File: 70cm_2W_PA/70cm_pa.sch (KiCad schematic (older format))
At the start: 47 parts, among them J3 Conn_01x02, U1 M68710L, U2 MIC5205YM5, U3 SN74LV1T08

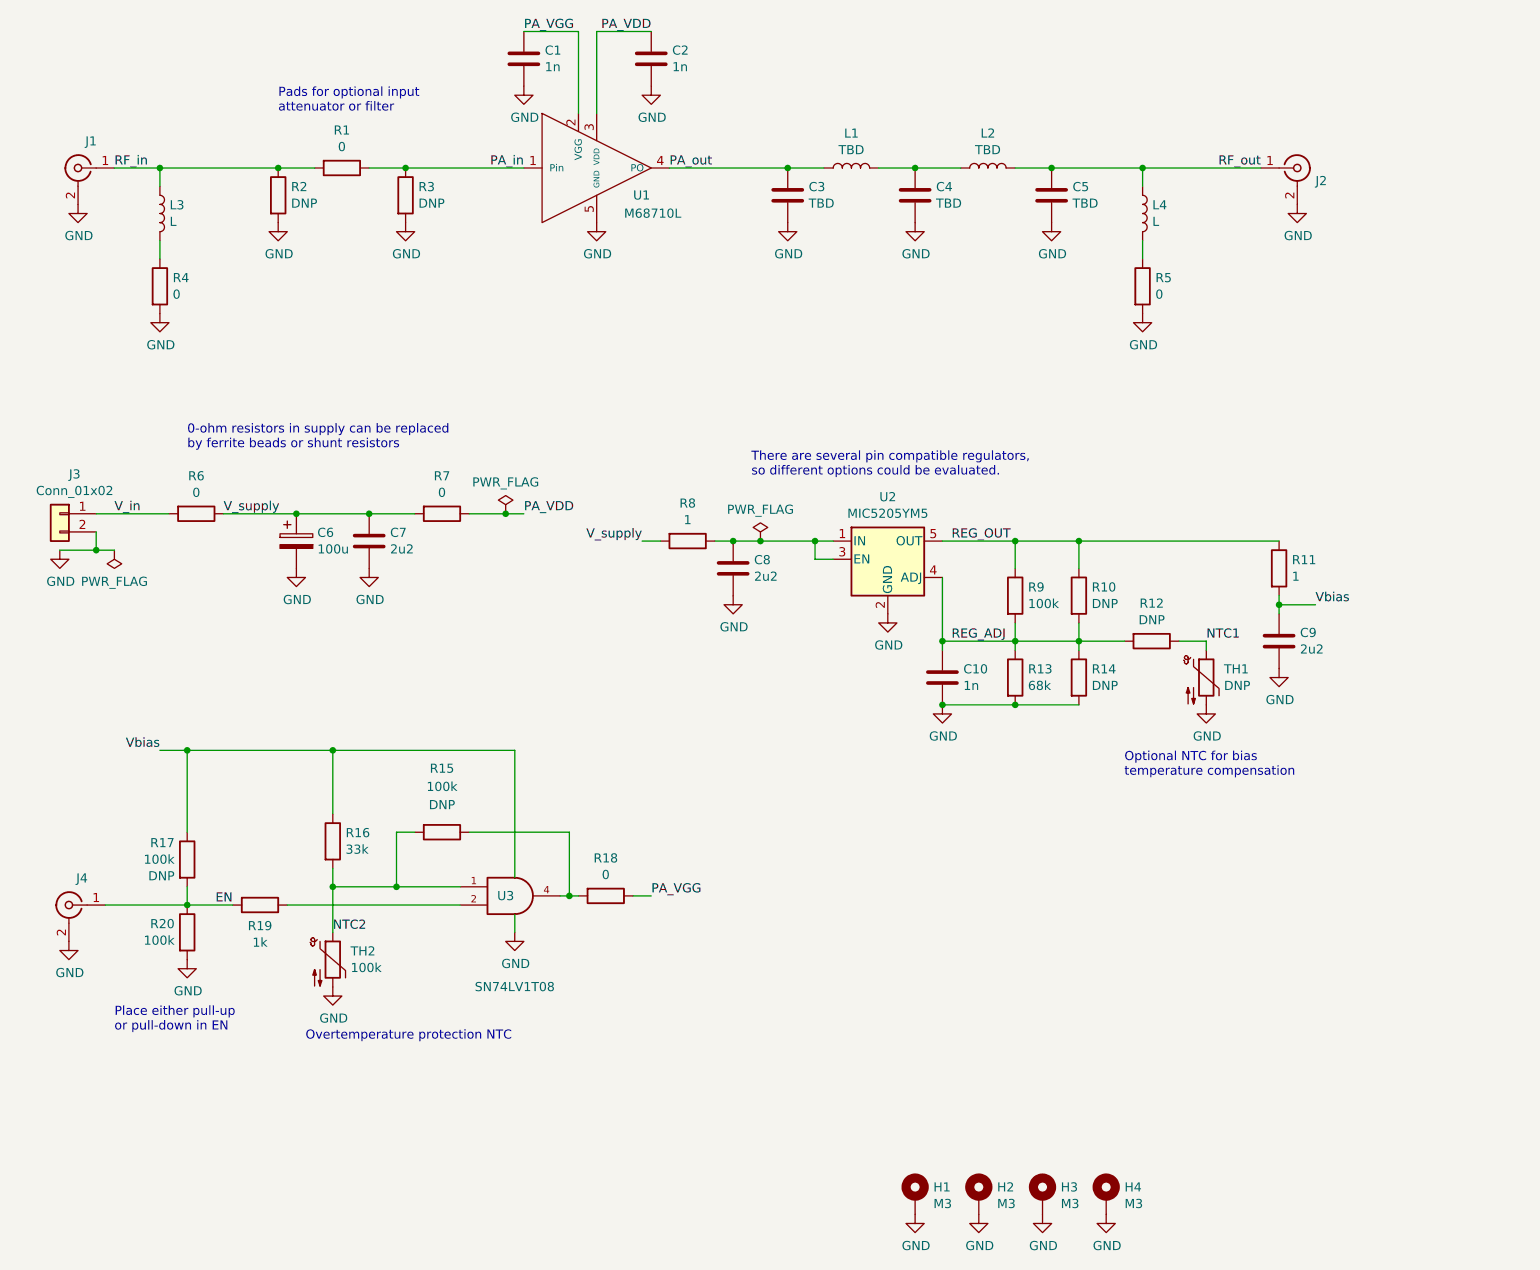
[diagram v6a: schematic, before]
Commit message: M68710L: Add more filtering and improve layout
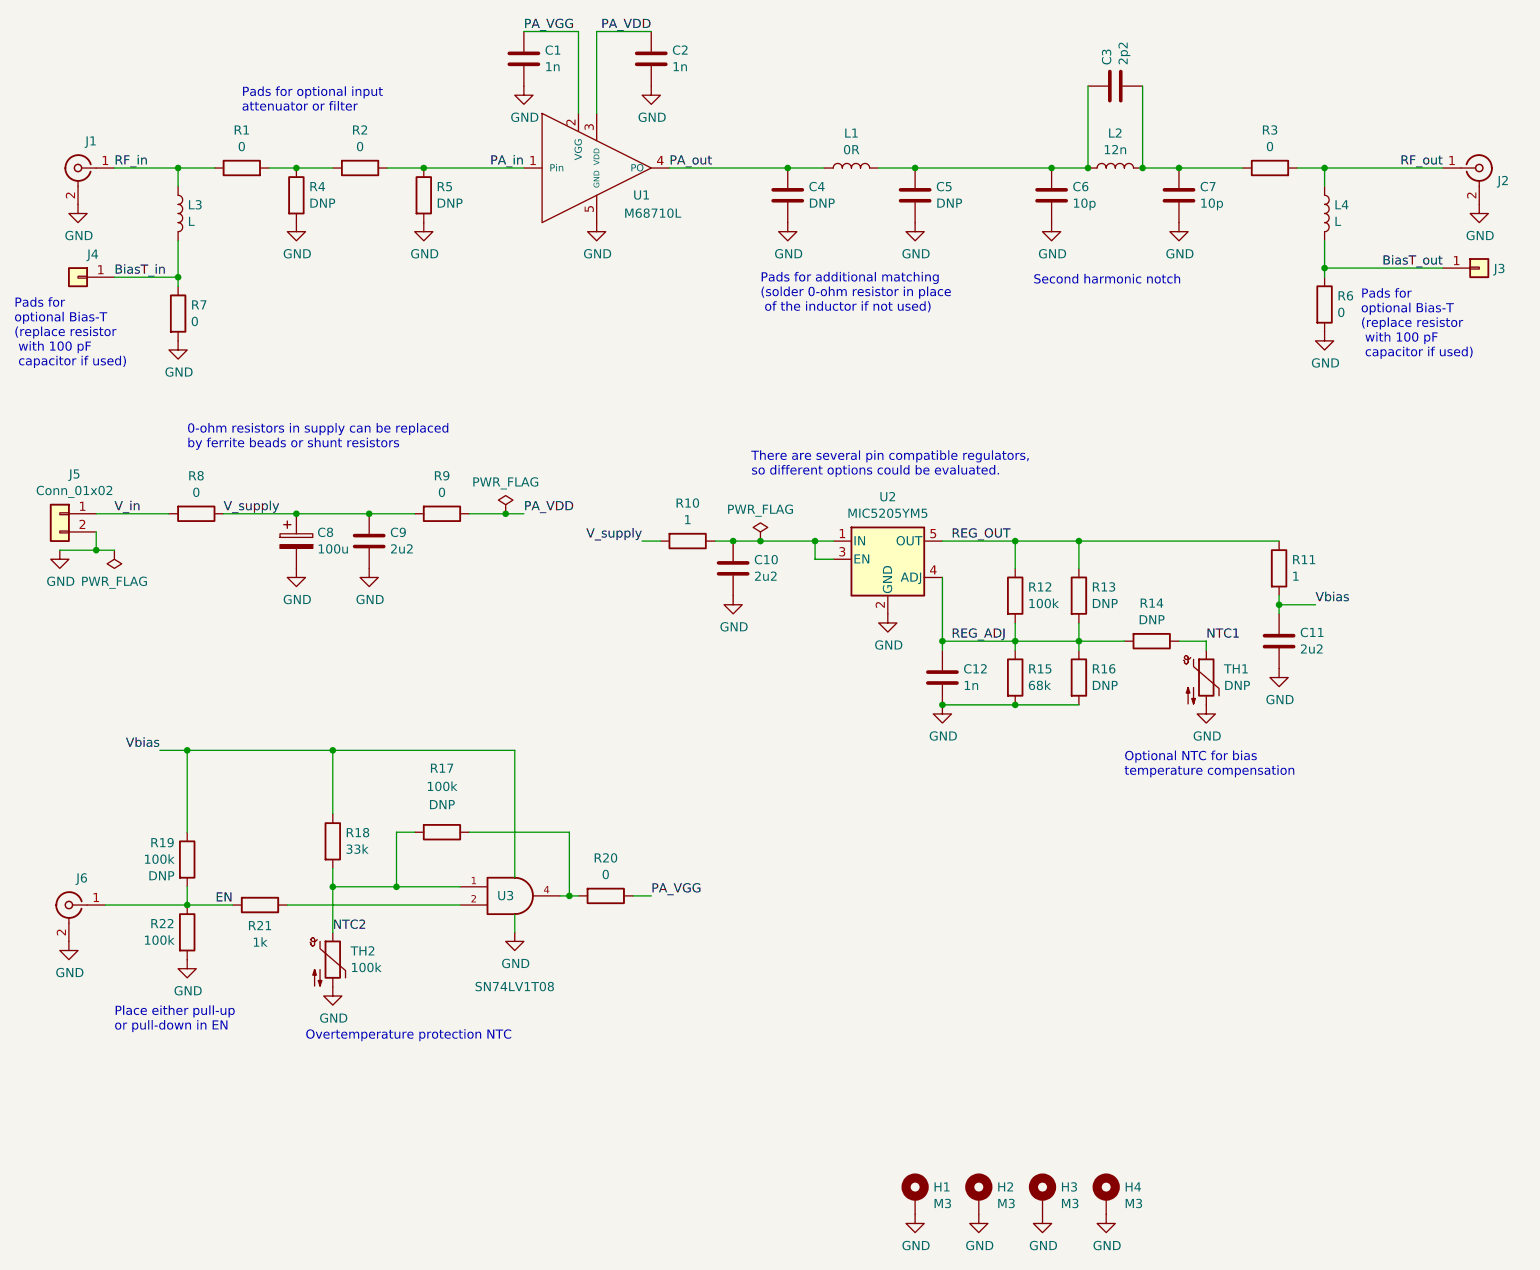
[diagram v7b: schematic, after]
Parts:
- added C3: 2p2, Capacitor_SMD:C_0805_2012Metric, symbol Device:C
- added C6: 10p, Capacitor_SMD:C_0805_2012Metric, symbol Device:C
- added J3, J4: ~, TestPoint:TestPoint_Pad_3.0x3.0mm, symbol Connector_Generic:Conn_01x01
- added R1, R3: 0, Resistor_SMD:R_0805_2012Metric, symbol Device:R
- C4: renamed from C3; value TBD -> ~; DNP (none) -> DNP
- C5: renamed from C4; value TBD -> ~; DNP (none) -> DNP
- C7: renamed from C5; value TBD -> 10p
- L1: value TBD -> 0R
- L2: value TBD -> 12n
- renumbered C8 to C10, C9 to C11, C10 to C12, C6 to C8, C7 to C9, J3 to J5, J4 to J6, R8 to R10, R9 to R12, R10 to R13, R12 to R14, R13 to R15, R14 to R16, R15 to R17, R16 to R18, R17 to R19, R1 to R2, R18 to R20, R19 to R21, R20 to R22, R2 to R4, R3 to R5, R5 to R6, R4 to R7, R6 to R8, R7 to R9
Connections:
- net GND: now also C6.2
- net RF_in: now also R1.1; no longer R2.2, R4.1
- net RF_out: now also R3.2; no longer C7.1, L2.2
- net BiasT_in: now reaches L3.2, R7.1
- net BiasT_in: now also J4.1 (Pin_1)
- net at C5.1, L1.2, L2.1: now also C3.1, C6.1
- net BiasT_out: now reaches L4.2, R6.1
- net BiasT_out: now also J3.1 (Pin_1)
- new net: R1.2, R2.2, R4.1
- new net: C3.2, C7.1, L2.2, R3.1
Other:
- note added: "Pads for additional matching\n(solder 0-ohm resistor in place\n of the inductor if not used)"
- note added: "Pads for\noptional Bias-T\n(replace resistor\n with 100 pF\n capacitor if used)"
- note added: "Second harmonic notch"
- moved on the sheet: C7, J2, L2, L3, L4, R2, R4, R5, R6, R7
